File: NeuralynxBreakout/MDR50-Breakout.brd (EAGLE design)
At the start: 58.4 x 57.1 mm, 3 parts, among them U1 10250-55H3PC

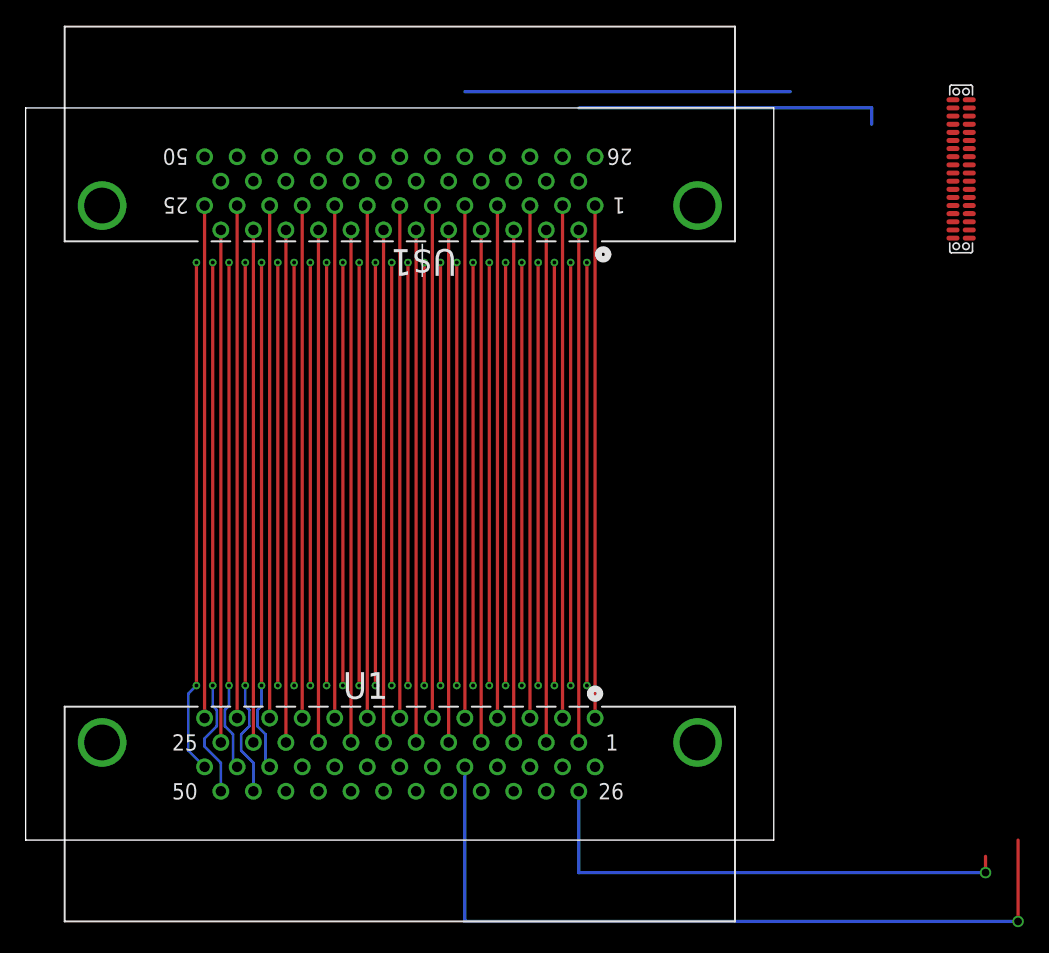
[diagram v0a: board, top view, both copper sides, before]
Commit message: Updated, almost finished interface board
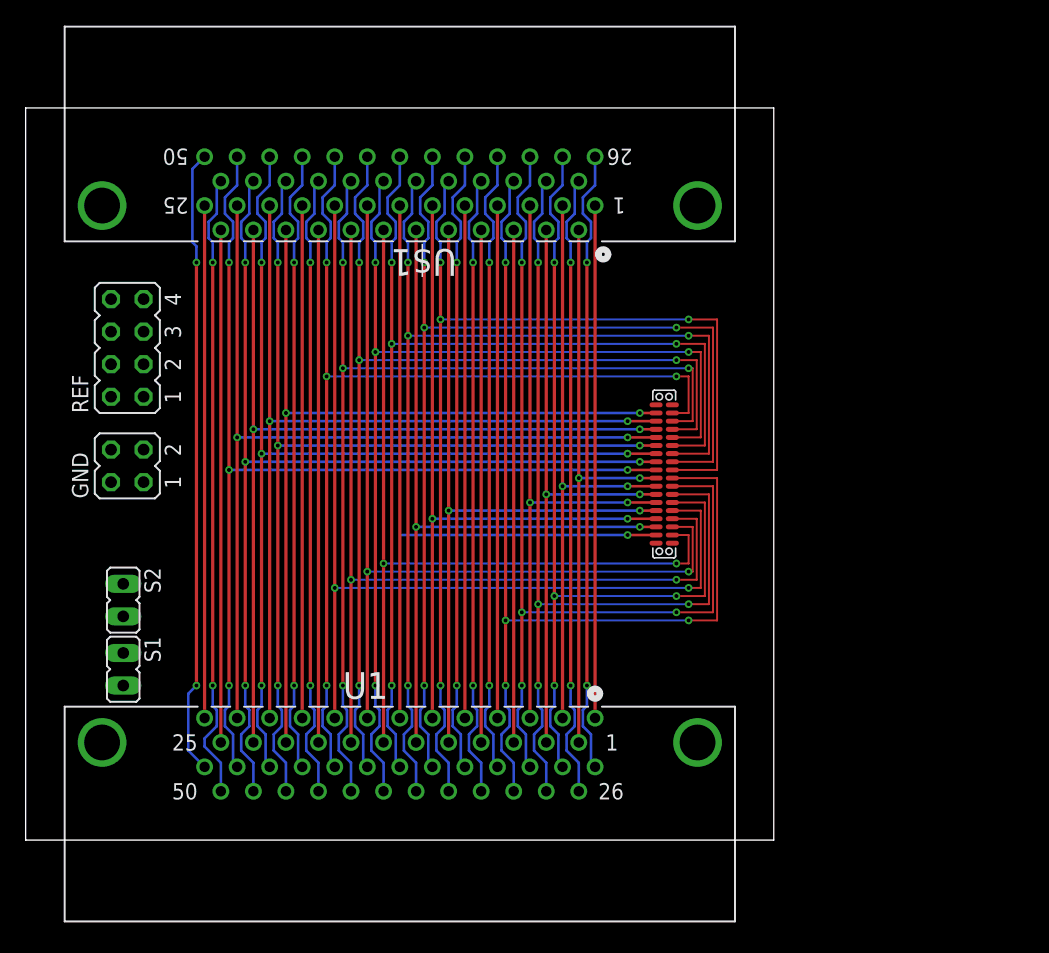
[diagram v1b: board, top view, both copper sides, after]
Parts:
- added GND: (no value), jumper:JP2Q
- added REF: (no value), jumper:JP4Q
- added S1, S2: (no value), jumper:JP1
- U$1: device Connectors:3M_10150-5242PC -> UsefulConnectors:3M_10150-5242PC
- U1: device Connectors:3M_10250-55H3PC -> UsefulConnectors:3M_10250-55H3PC
- moved U$2 27.7 mm to (49.2, 34.0), turned to 270 degrees
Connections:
- new net INTANGND: GND.1, GND.3, U$2.P$1, U$2.P$19
- new net INTANREF: U$2.P$18
- new net N$1: REF.1, REF.3, REF.5, REF.7, U$2.P$36
- net D10: now also U$2.P$14
- net D11: now also U$2.P$15
- net D12: now also U$2.P$16
- net D13: now also U$2.P$17
- net D14: now also U$2.P$20
- net D15: now also U$2.P$21
- net D16: now also U$2.P$22
- net D17: now also U$2.P$23
- net D18: now also S2.1
- net D19: now also S2.2
- net D2: now also U$2.P$10
- net D20: now also U$2.P$2
- net D21: now also U$2.P$3
- net D22: now also U$2.P$4
- net D23: now also U$2.P$5
- net D27: now also REF.2; no longer U$2.P$18, U$2.P$36
- net D28: now also U$2.P$24
- net D29: now also U$2.P$25
- net D3: now also U$2.P$11
- net D30: now also U$2.P$26
- net D31: now also U$2.P$27
- net D34: now also GND.2; no longer U$2.P$1, U$2.P$19
- net D35: now also U$2.P$28
- net D36: now also U$2.P$29
- net D37: now also U$2.P$30
- net D38: now also U$2.P$31
- net D39: now also U$2.P$32
- net D4: now also U$2.P$12
- net D40: now also U$2.P$33
- net D41: now also U$2.P$34
- net D42: now also U$2.P$35
- net D43: now also GND.4
- net D44: now also REF.8
- net D45: now also U$2.P$6
- net D46: now also U$2.P$7
- net D47: now also U$2.P$8
- net D48: now also U$2.P$9
- net D5: now also U$2.P$13
- net D6: now also REF.4
- net D7: now also S1.1
- net D8: now also S1.2
- net D9: now also REF.6
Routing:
- net D34: track 120.0 -> 48.9 mm, vias 3 -> 2
- net D35: track 33.0 -> 85.8 mm, vias 2 -> 4
- net D36: track 33.0 -> 85.1 mm, vias 2 -> 4
- net D37: track 33.0 -> 84.5 mm, vias 2 -> 4
- net D38: track 33.0 -> 83.9 mm, vias 2 -> 4
- net D39: track 33.0 -> 83.2 mm, vias 2 -> 4
- net D40: track 33.0 -> 82.6 mm, vias 2 -> 4
- net D41: track 33.0 -> 82.0 mm, vias 2 -> 4
- net D42: track 33.0 -> 81.3 mm, vias 2 -> 4
- net D27: track 96.5 -> 48.9 mm, vias 3 -> 2
- net D31: track 33.0 -> 80.1 mm, vias 2 -> 4
- net D45: track 33.0 -> 78.5 mm, vias 2 -> 4
- net D30: track 33.0 -> 76.9 mm, vias 2 -> 4
- net D48: track 39.9 -> 82.3 mm, vias 2 -> 4
- net D29: track 33.0 -> 73.7 mm, vias 2 -> 4
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
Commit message: Updated Neuralynx breakout board before manufacturing
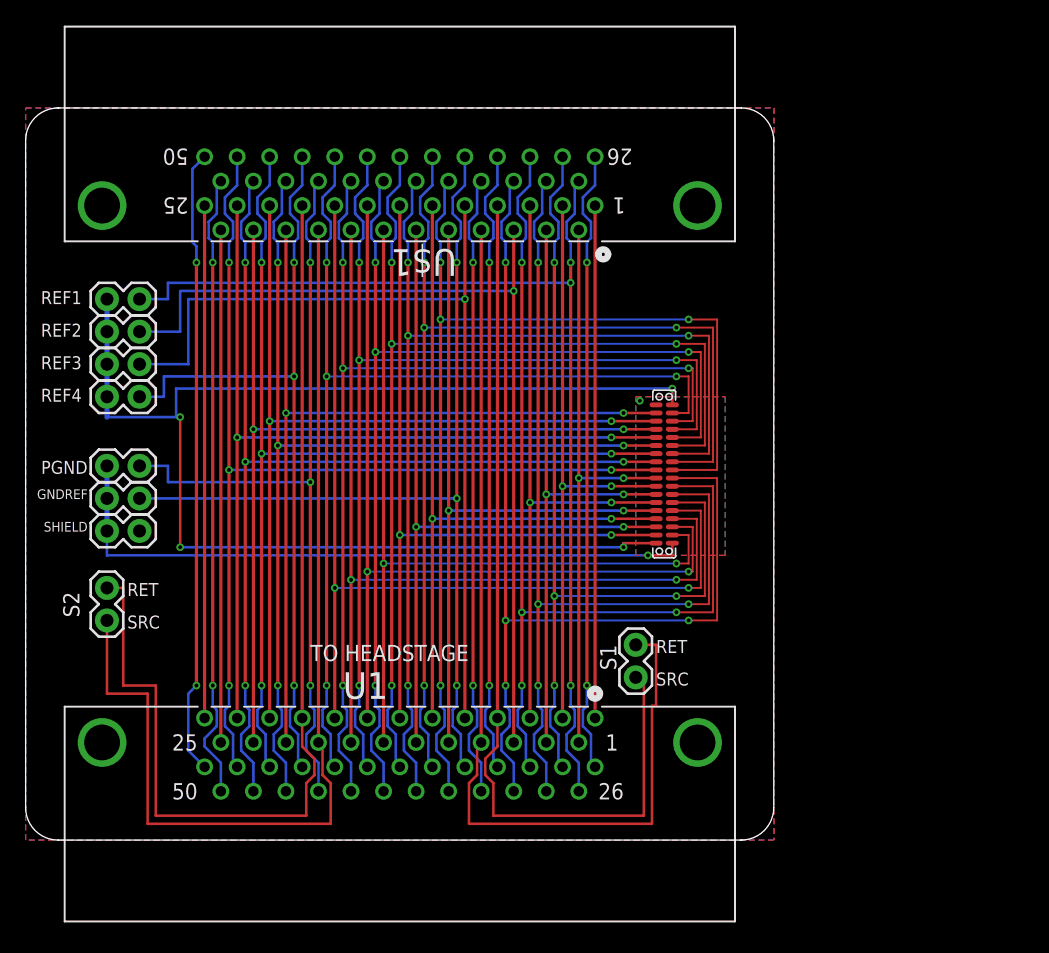
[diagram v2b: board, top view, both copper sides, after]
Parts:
- removed GND: (no value), jumper:JP2Q
- removed REF: (no value), jumper:JP4Q
- added GNDREF, PGND, REF1, REF2, REF3, REF4, SHIELD: (no value), SparkFun:1X02
- S1, S2: device jumper:JP1 -> SparkFun:1X02
- moved S1 40.0 mm to (47.6, 12.7), turned to 90 degrees
- moved S2 2.03 mm to (6.35, 17.1), turned to 90 degrees
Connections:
- removed net N$1: REF.1, REF.3, REF.5, REF.7, U$2.P$36
- new net GND: SHIELD.1, U$1.51, U$1.52, U1.51, U1.52
- net D27: now also REF1.2; no longer REF.2
- net D34: now also GNDREF.1; no longer GND.2
- net D43: now also PGND.1; no longer GND.4
- net D44: now also REF4.2; no longer REF.8
- net D6: now also REF2.2; no longer REF.4
- net D9: now also REF3.2; no longer REF.6
- net INTANGND: now also GNDREF.2, PGND.2, SHIELD.2; no longer GND.1, GND.3
- net INTANREF: now also REF1.1, REF2.1, REF3.1, REF4.1, U$2.P$36
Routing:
- net INTANREF: track 0.00 -> 104.8 mm, vias 0 -> 4
- net INTANGND: track 0.00 -> 52.1 mm, vias 0 -> 2
- net D19: track 40.0 -> 81.6 mm
- net D18: track 40.0 -> 80.1 mm
- net D8: track 40.0 -> 76.9 mm
- net D27: track 48.9 -> 83.9 mm, vias 2 -> 3
- net D6: track 40.0 -> 72.4 mm, vias 0 -> 1
- net D7: track 40.0 -> 71.1 mm
- net D9: track 40.0 -> 70.5 mm, vias 0 -> 1
- net D34: track 48.9 -> 73.7 mm, vias 2 -> 3
- net D43: track 48.9 -> 63.5 mm, vias 2 -> 3
- net D44: track 48.9 -> 62.6 mm, vias 2 -> 3
- net D13: vias 1 -> 2
- added copper zone on layer 1, net GND
- added copper zone on layer 16, net GND
- added copper zone on layer 1, net INTANGND
- added copper zone on layer 16, net INTANGND
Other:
- outline, holes or cut-outs redrawn
- board text added: "RET"
- board text added: "SRC"
- board text added: "TO HEADSTAGE"
